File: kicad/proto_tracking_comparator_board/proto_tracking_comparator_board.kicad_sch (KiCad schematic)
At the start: 19 parts, among them U1 TLV3542, U2 MCP6566

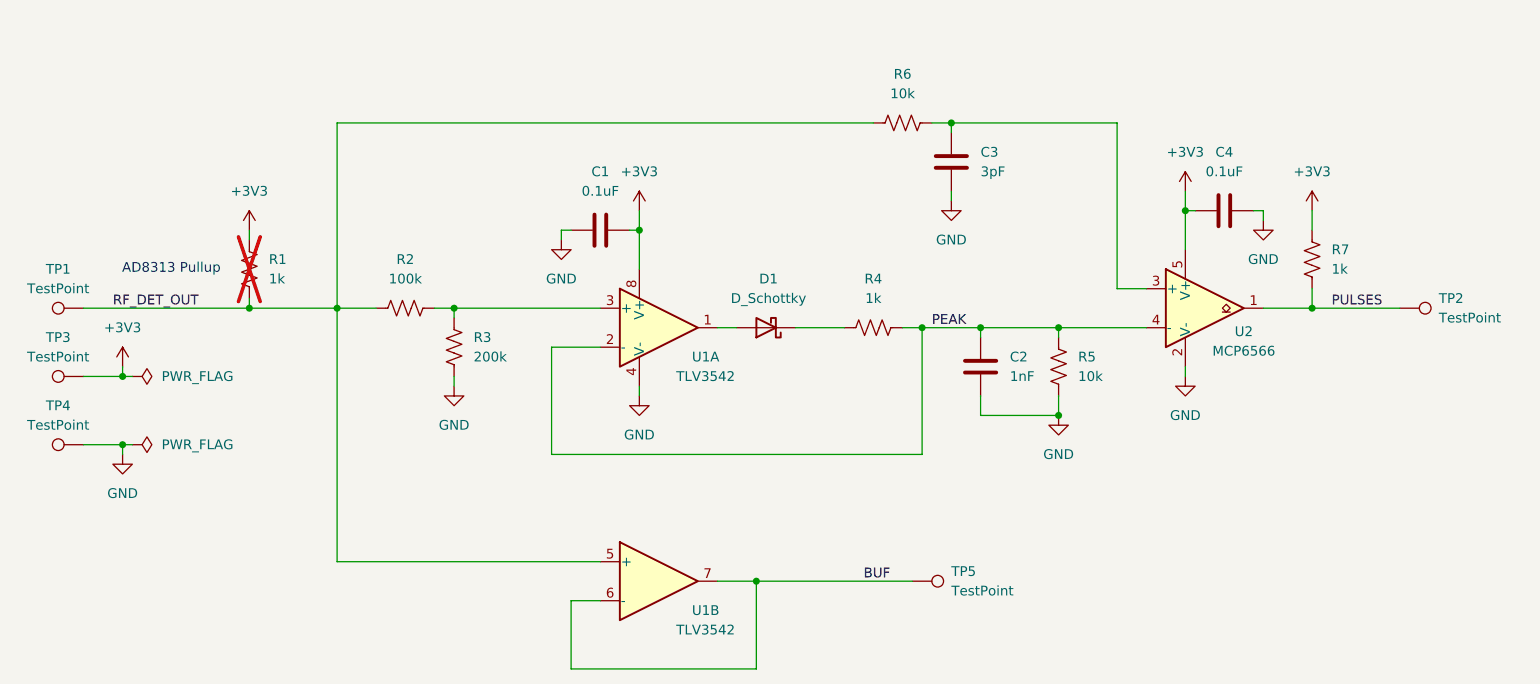
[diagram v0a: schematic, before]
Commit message: Save bodge board rev B and additional sims
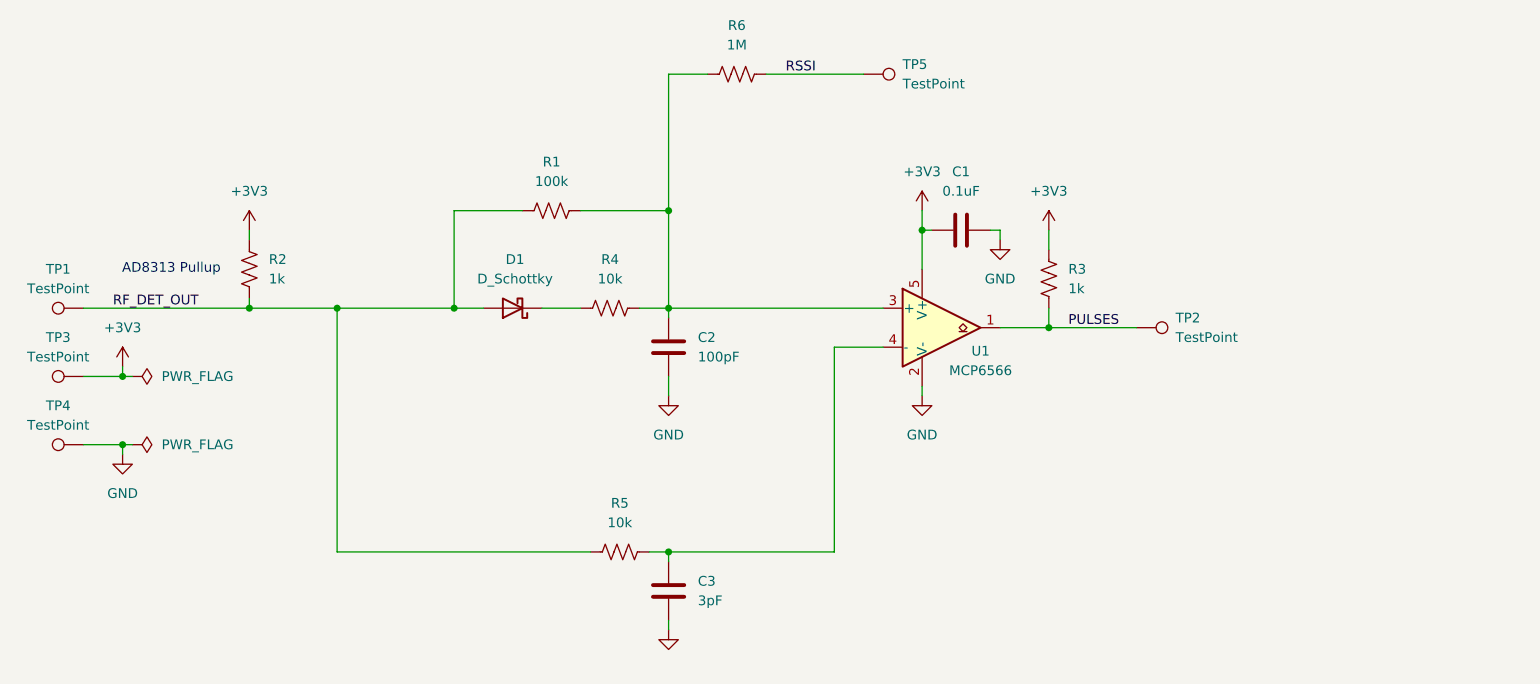
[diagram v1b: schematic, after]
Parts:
- removed C1: 0.1uF, Capacitor_SMD:C_0603_1608Metric, symbol Device:C
- removed R2: 100k, Resistor_SMD:R_0603_1608Metric, symbol Device:R_US
- removed R3: 200k, Resistor_SMD:R_0603_1608Metric, symbol Device:R_US
- removed R5: 10k, Resistor_SMD:R_0603_1608Metric, symbol Device:R_US
- removed U1: TLV3542, Package_SO:VSSOP-8_3.0x3.0mm_P0.65mm, symbol Custom_Amplifier_Operational:TLV3542
- added R1: 100k, Resistor_SMD:R_0603_1608Metric, symbol Device:R_US
- added R6: 1M, Resistor_SMD:R_0603_1608Metric, symbol Device:R_US
- C2: value 1nF -> 100pF
- D1: footprint Diode_SMD:D_SMA -> Custom_Diode:D_0402_1005Metric
- R2: renamed from R1; now fitted
- R4: value 1k -> 10k
- renumbered C4 to C1, R7 to R3, R6 to R5, U2 to U1
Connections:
- net RF_DET_OUT: now also D1.2 (A), R1.1
- net at C3.1, R5.2: now also U1.4 (-); no longer U1.3 (+)
- net BUF renamed RSSI
- net RSSI: now also R6.2
- net PEAK: no longer names the net of C2.1, R4.2
- net PEAK: now also U1.3 (+), R1.2, R6.1; no longer U1.4 (-)
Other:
- moved on the sheet: C1, C3, D1, R3, R5, TP2, U1

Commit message: Data slicer rev A
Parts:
- removed C2: 100pF, Capacitor_SMD:C_0603_1608Metric, symbol Device:C
- removed R3: 1k, Resistor_SMD:R_0603_1608Metric, symbol Device:R_US
- removed R4: 10k, Resistor_SMD:R_0603_1608Metric, symbol Device:R_US
- removed R6: 1M, Resistor_SMD:R_0603_1608Metric, symbol Device:R_US
- removed TP3: TestPoint, TestPoint:TestPoint_Pad_1.0x1.0mm, symbol Connector:TestPoint
- removed U1: MCP6566, Package_TO_SOT_SMD:SOT-353_SC-70-5, symbol Comparator:MCP6566
- added D2: D_Schottky, Custom_Diode:D_0402_1005Metric, symbol Device:D_Schottky
- added R7: 200k, Resistor_SMD:R_0603_1608Metric, symbol Device:R_US
- added TP6, TP7: TestPoint, TestPoint:TestPoint_Pad_1.0x1.0mm, symbol Connector:TestPoint
- C3: value 3pF -> 1nF
- R1: value 100k -> 10k
- R2: value 1k -> 100k
- R5: value 10k -> 100k
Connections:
- net PULSES is gone; now on net TL_FLOOR: TP2.1
- net GND: now also C1.2, R7.1; no longer C1.1
- net RSSI: now also C3.1, D1.1 (K), R5.2, D2.1 (K)
- net TL_FLOOR: now reaches R1.2
- net +3V3 renamed TL_LO
- net TL_LO: now also R7.2, TP7.1; no longer C1.2
- removed net RF_DET_OUT: D1.2 (A), R1.1, R2.2, R5.1, TP1.1
- new net: C1.1, D2.2 (A), R1.1
- new net RF_LEVEL: D1.2 (A), TP1.1
- new net TL_HI: R2.2, R5.1, TP6.1
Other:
- note removed: "AD8313 Pullup"
- moved on the sheet: D1
